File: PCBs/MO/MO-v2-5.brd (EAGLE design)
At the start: 100 x 100 mm, 51 parts, among them J1 Teensy-5V, J12 RPi-Shutdown, J17 +5V IN (Main), J3 +5V OUT (to Pi), J4 ACTUATORS, J5 +5V IN (Pi), SW2 500SSP1S2M2QEA, U1 ATTINY85DIP08, U2 A2982

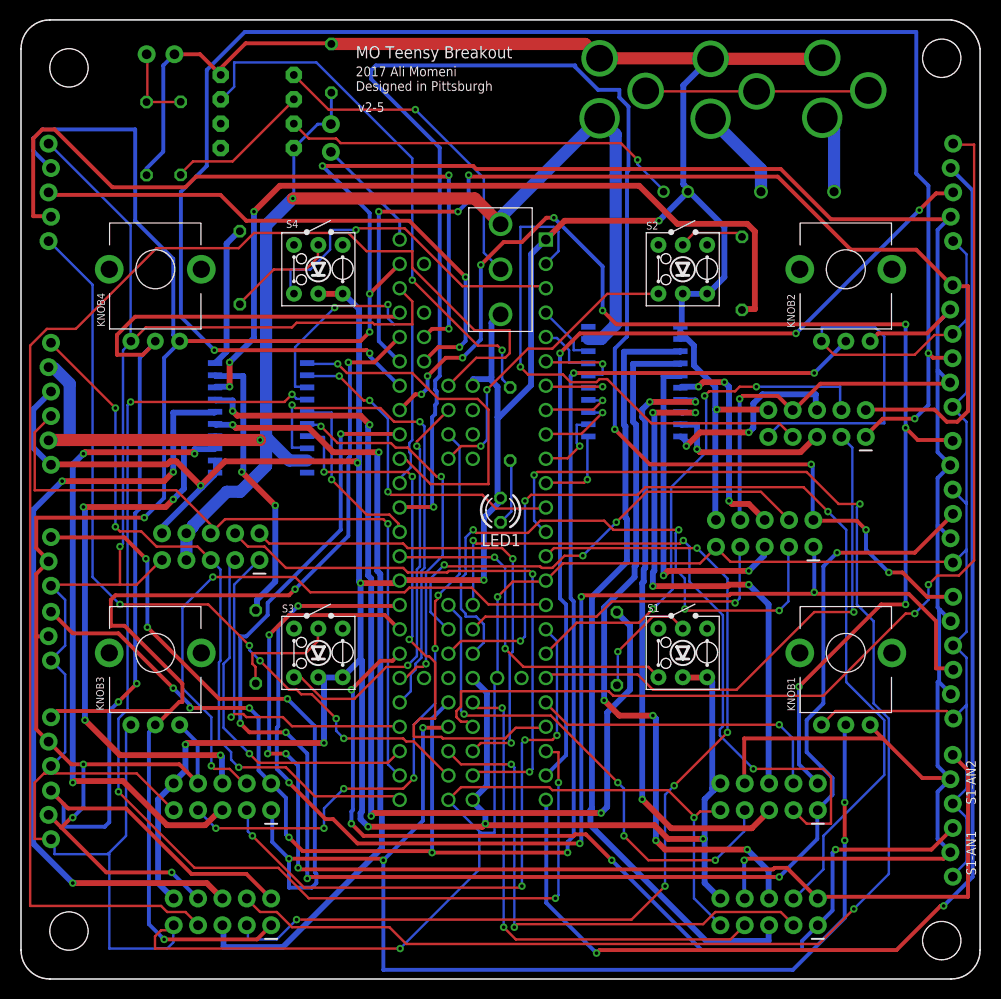
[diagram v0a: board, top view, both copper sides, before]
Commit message: newly routed v2-5 breakout
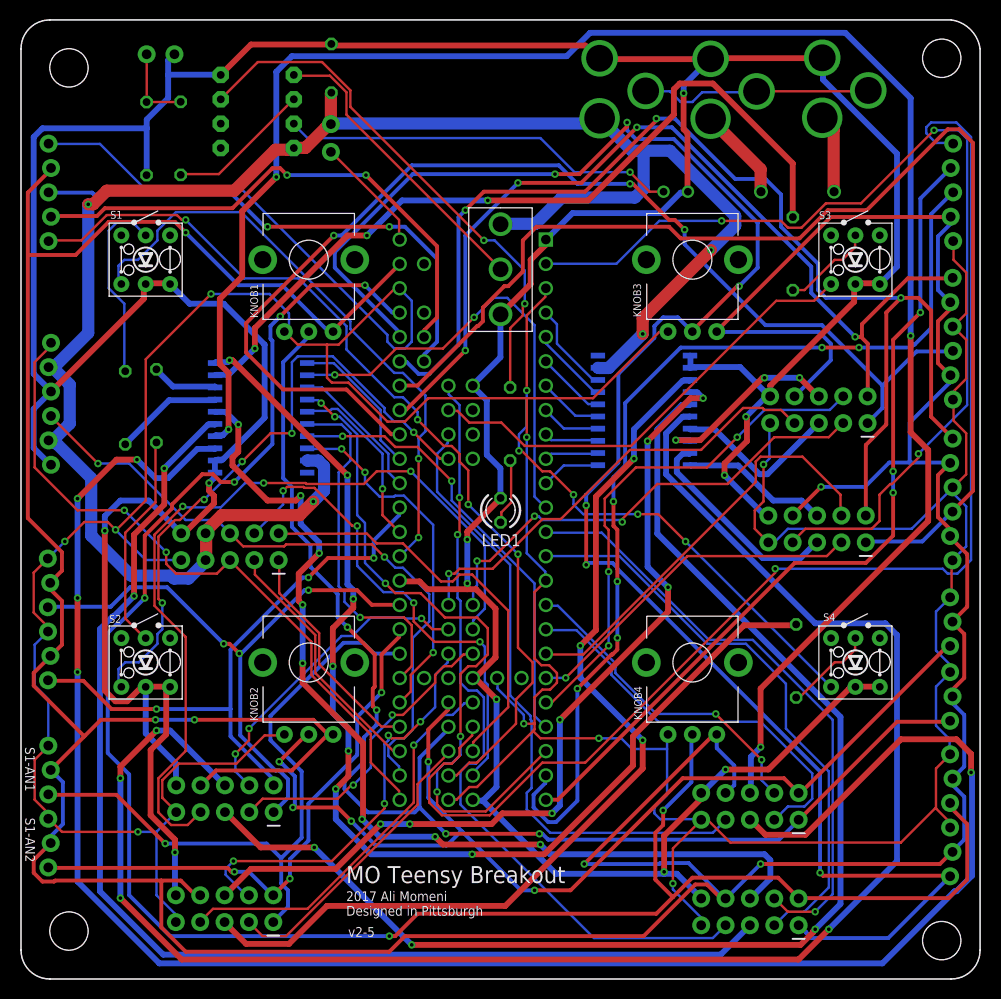
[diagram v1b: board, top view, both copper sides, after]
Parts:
- moved S2-AN3 95.6 mm to (2.92, 43.8), turned to 270 degrees
- moved S1-AN1 95.0 mm to (2.97, 24.3), turned to 270 degrees
- moved S5-AN9 94.4 mm to (97.0, 32.0), turned to 270 degrees
- moved S6-AN12 94.4 mm to (97.0, 23.4), turned to 270 degrees
- moved S5-AN10 94.2 mm to (97.0, 39.8), turned to 270 degrees
- moved S6-AN11 94.2 mm to (97.0, 15.8), turned to 270 degrees
- moved S2-AN4 94.1 mm to (2.94, 36.2), turned to 270 degrees
- moved S1-AN2 94.1 mm to (2.97, 16.7), turned to 270 degrees
- moved R7 71.0 mm to (80.8, 33.2)
- moved KNOB1 69.4 mm to (30.0, 75.0)
- moved KNOB2 69.4 mm to (30.0, 33.0)
- moved KNOB3 69.4 mm to (70.0, 75.0)
- moved KNOB4 69.4 mm to (70.0, 33.0)
- moved R6 69.4 mm to (80.5, 75.6)
- moved S1 69.4 mm to (13.0, 75.0)
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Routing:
- net PWM_4: track 22.0 -> 178.5 mm, vias 3 -> 4
- net PWM_10: track 60.9 -> 193.4 mm
- net PWM_9: track 67.4 -> 199.9 mm, vias 3 -> 5
- net PWM_16: track 14.9 -> 118.4 mm, vias 0 -> 7
- net AN4: track 163.2 -> 61.6 mm, vias 5 -> 3
- net PWM_3: track 34.9 -> 133.6 mm, vias 2 -> 3
- net PWM_13: track 105.7 -> 11.3 mm, vias 4 -> 0
- net BTN12: track 154.0 -> 63.6 mm, vias 3 -> 1
- net AN12: track 126.3 -> 208.5 mm, vias 2 -> 6
- net PWM_14: track 85.7 -> 6.97 mm, vias 3 -> 0
- net AN3: track 139.3 -> 63.2 mm, vias 5 -> 3
- net AN11: track 118.3 -> 190.4 mm, vias 3 -> 6
- net AN2: track 128.7 -> 57.8 mm, vias 4 -> 3
- net LED6: track 147.1 -> 81.3 mm, vias 0 -> 2
- net BTN2: track 102.8 -> 43.4 mm, vias 3 -> 4
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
